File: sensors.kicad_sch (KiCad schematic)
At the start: 0 parts

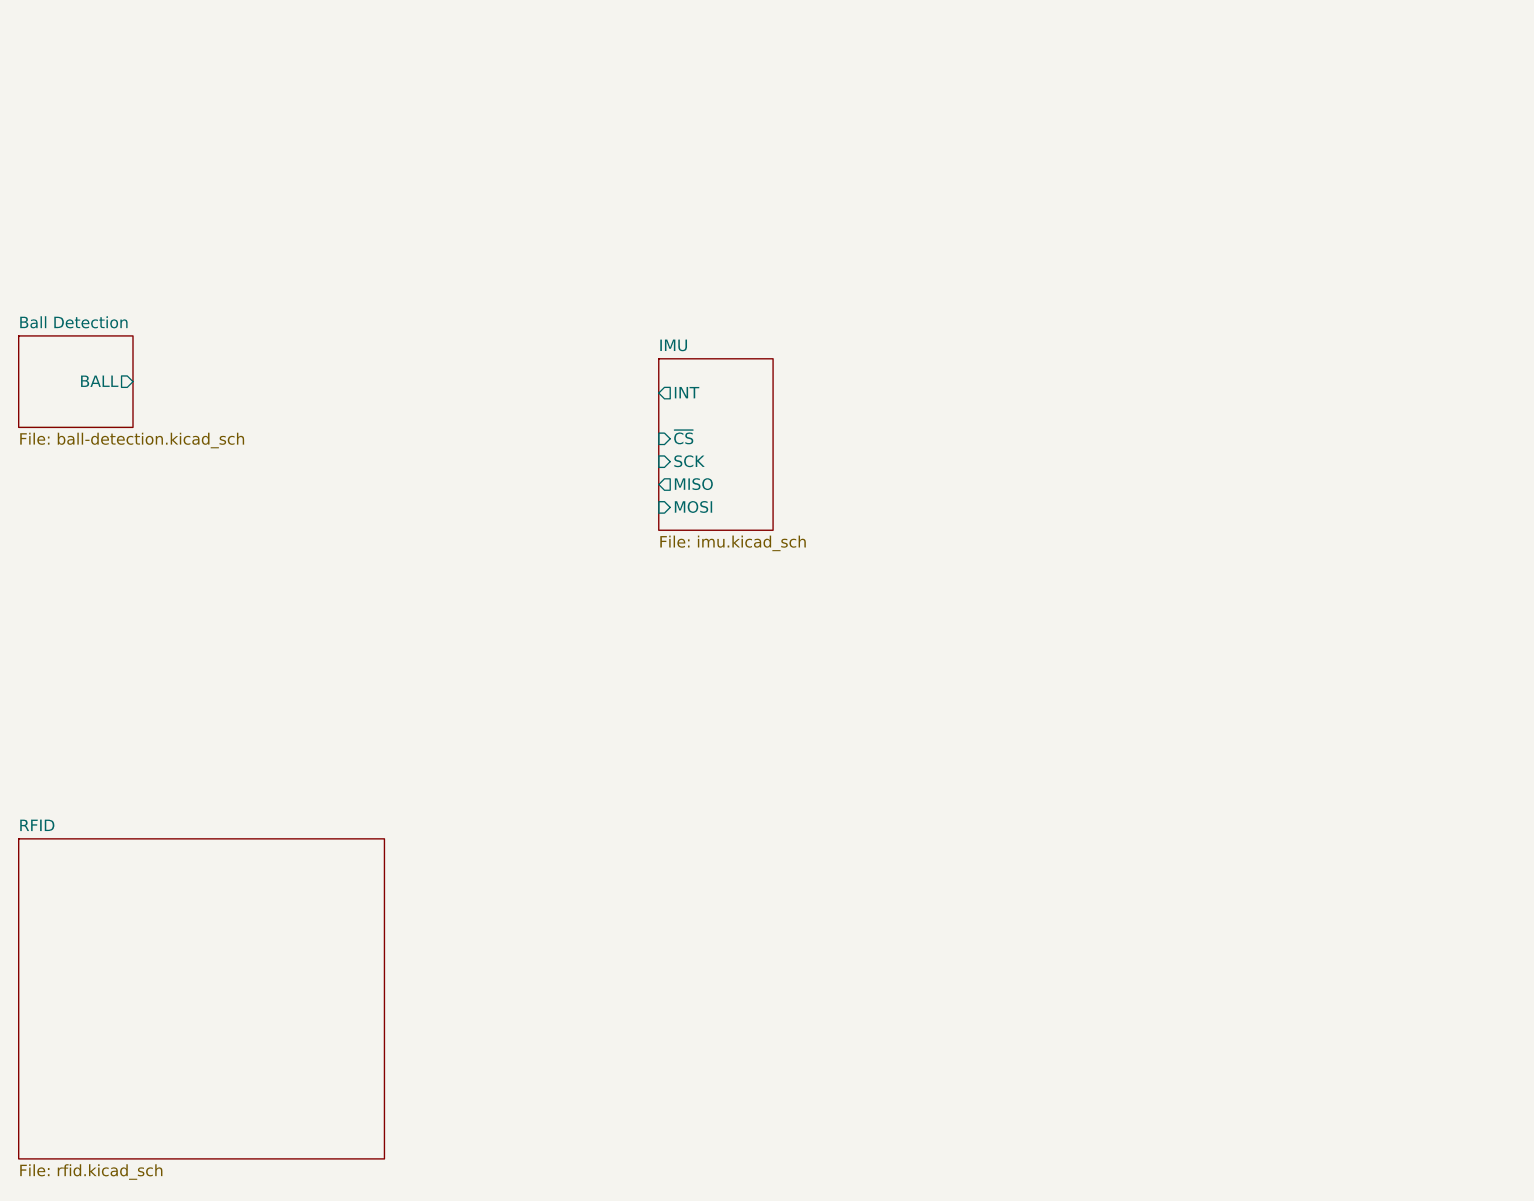
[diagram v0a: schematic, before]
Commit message: Move sensors to one sheet.
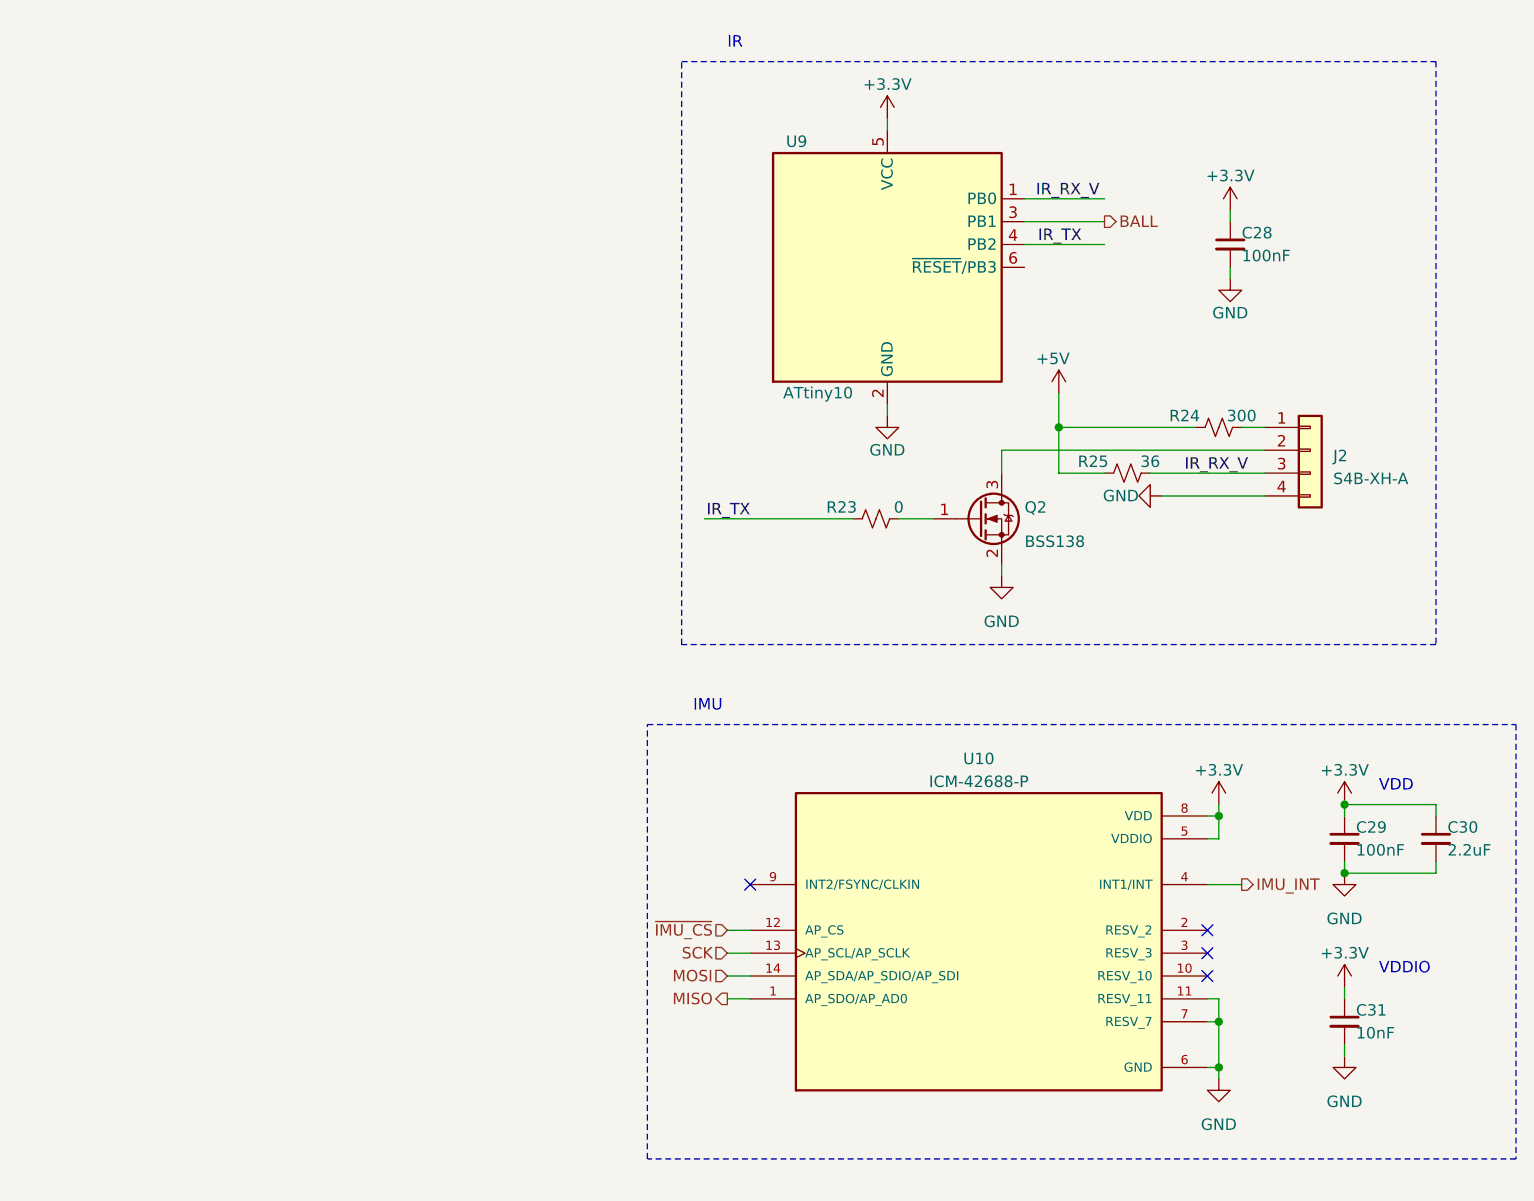
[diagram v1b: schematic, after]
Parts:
- added C28, C29: 100nF, symbol Device:C_Small
- added C30: 2.2uF, symbol Device:C_Small
- added C31: 10nF, symbol Device:C_Small
- added J2: S4B-XH-A, symbol Connector_Generic:Conn_01x04
- added Q2: BSS138, Package_TO_SOT_SMD:SOT-23, symbol Transistor_FET:BSS138
- added R23: 0, symbol Device:R_Small_US
- added R24: 300, symbol Device:R_Small_US
- added R25: 36, symbol Device:R_Small_US
- added U10: ICM-42688-P, ICM-42688-P:PQFN50P300X250X97-14N, symbol ICM-42688-P:ICM-42688-P
- added U9: ATtiny10, Package_TO_SOT_SMD:SOT-23-6, symbol MCU_Microchip_ATtiny:ATtiny10-TS
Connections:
- new net: J2.1 (Pin_1), R24.2
- new net: J2.2 (Pin_2), Q2.3 (D)
- new net: Q2.1 (G), R23.2
- new net +3.3V: C28.1, C29.1, C30.1, C31.1, U10.5 (VDDIO), U10.8 (VDD), U9.5 (VCC)
- new net +5V: R24.1, R25.1
- new net BALL: U9.3 (PB1)
- new net GND: C28.2, C29.2, C30.2, C31.2, J2.4 (Pin_4), Q2.2 (S), U10.11 (RESV_11), U10.6 (GND), U10.7 (RESV_7), U9.2 (GND)
- new net IMU_INT: U10.4 (INT1/INT)
- new net IR_RX_V: J2.3 (Pin_3), R25.2, U9.1 (PB0)
- new net IR_TX: R23.1, U9.4 (PB2)
- new net MISO: U10.1 (AP_SDO/AP_AD0)
- new net MOSI: U10.14 (AP_SDA/AP_SDIO/AP_SDI)
- new net SCK: U10.13 (AP_SCL/AP_SCLK)
- new net ~{IMU_CS}: U10.12 (AP_CS)
- no-connect marks 0 -> 4
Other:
- removed sheet Ball Detection
- removed sheet IMU
- removed sheet RFID
- note added: "IMU"
- note added: "IR"
- note added: "VDD"
- note added: "VDDIO"

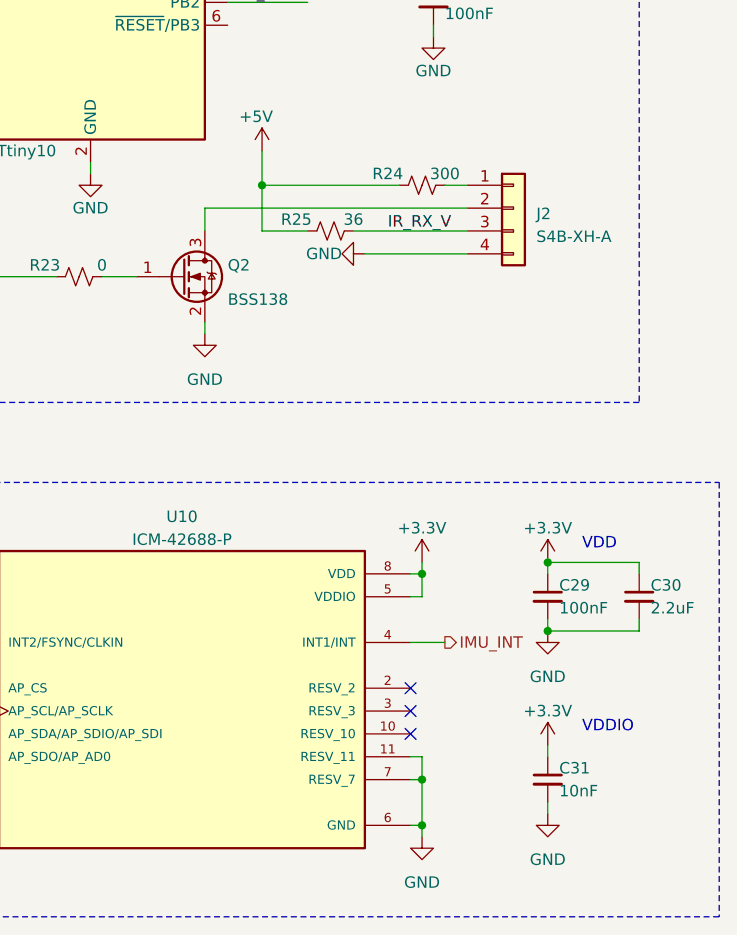
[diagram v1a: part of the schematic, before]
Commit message: Add RP2040
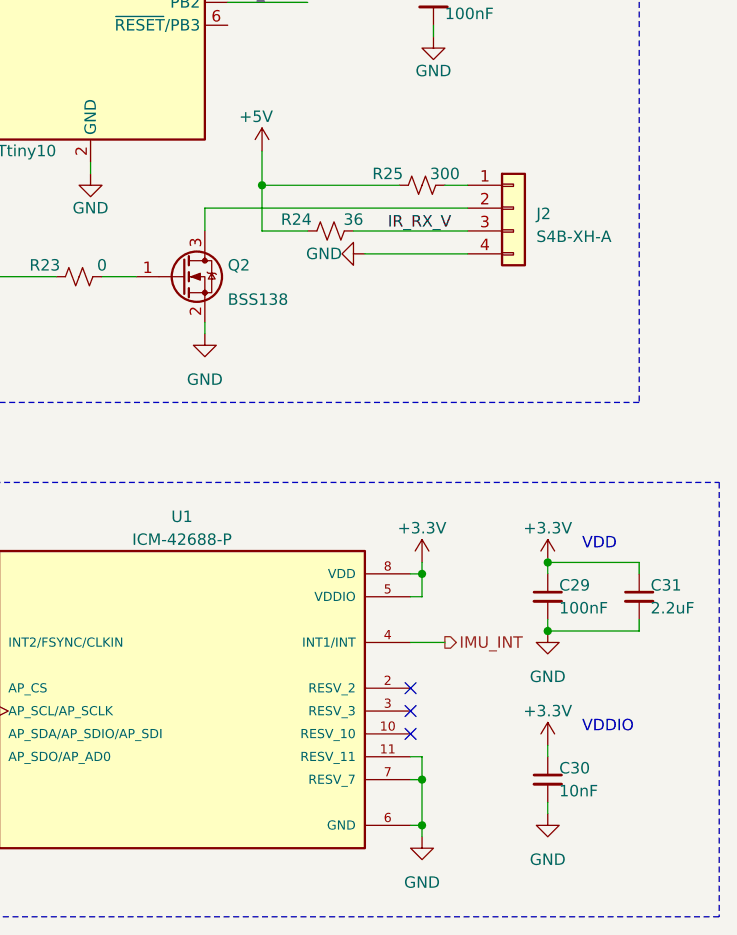
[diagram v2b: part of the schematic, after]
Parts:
- renumbered C31 to C30, C30 to C31, R25 to R24, R24 to R25, U10 to U1
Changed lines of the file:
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@@
   (symbol (lib_id "Device:R_Small_US") (at 217.17 76.2 90) (unit 1)
     (in_bom yes) (on_board yes) (dnp no)
-    (property "Reference" "R25" (at 213.36 74.93 90)
+    (property "Reference" "R24" (at 213.36 74.93 90)
       (effects (font (size 1.27 1.27)))
     )
@@
   (symbol (lib_id "Device:C_Small") (at 241.3 137.16 0) (unit 1)
     (in_bom yes) (on_board yes) (dnp no)
-    (property "Reference" "C31" (at 242.57 135.89 0)
+    (property "Reference" "C30" (at 242.57 135.89 0)
       (effects (font (size 1.27 1.27)) (justify left))
     )
@@
   (symbol (lib_id "power:+3.3V") (at 190.5 36.83 0) (unit 1)
     (in_bom yes) (on_board yes) (dnp no) (fields_autoplaced)
-    (property "Reference" "#PWR062" (at 190.5 40.64 0)
+    (property "Reference" "#PWR060" (at 190.5 40.64 0)
       (effects (font (size 1.27 1.27)) hide)
     )
@@
   (symbol (lib_id "power:GND") (at 203.2 87.63 0) (unit 1)
     (in_bom yes) (on_board yes) (dnp no) (fields_autoplaced)
-    (property "Reference" "#PWR060" (at 203.2 93.98 0)
+    (property "Reference" "#PWR062" (at 203.2 93.98 0)
       (effects (font (size 1.27 1.27)) hide)
     )
@@
   (symbol (lib_id "Device:R_Small_US") (at 227.33 71.12 90) (unit 1)
     (in_bom yes) (on_board yes) (dnp no)
-    (property "Reference" "R24" (at 223.52 69.85 90)
+    (property "Reference" "R25" (at 223.52 69.85 90)
       (effects (font (size 1.27 1.27)))
     )
@@
   (symbol (lib_id "Device:C_Small") (at 251.46 116.84 0) (unit 1)
     (in_bom yes) (on_board yes) (dnp no)
-    (property "Reference" "C30" (at 252.73 115.57 0)
+    (property "Reference" "C31" (at 252.73 115.57 0)
       (effects (font (size 1.27 1.27)) (justify left))
     )
@@
   (symbol (lib_id "ICM-42688-P:ICM-42688-P") (at 200.66 127 0) (unit 1)
     (in_bom yes) (on_board yes) (dnp no) (fields_autoplaced)
-    (property "Reference" "U10" (at 200.66 107.95 0)
+    (property "Reference" "U1" (at 200.66 107.95 0)
       (effects (font (size 1.27 1.27)))
     )
@@
   (symbol (lib_id "power:GND") (at 220.98 78.74 270) (unit 1)
     (in_bom yes) (on_board yes) (dnp no)
-    (property "Reference" "#PWR061" (at 214.63 78.74 0)
+    (property "Reference" "#PWR064" (at 214.63 78.74 0)
       (effects (font (size 1.27 1.27)) hide)
     )
@@
   (symbol (lib_id "power:GND") (at 190.5 69.85 0) (unit 1)
     (in_bom yes) (on_board yes) (dnp no)
-    (property "Reference" "#PWR064" (at 190.5 76.2 0)
-      (effects (font (size 1.27 1.27)) hide)
-    )
+    (property "Reference" "#PWR061" (at 190.5 76.2 0)
+      (effects (font (size 1.27 1.27)) hide)
+    )

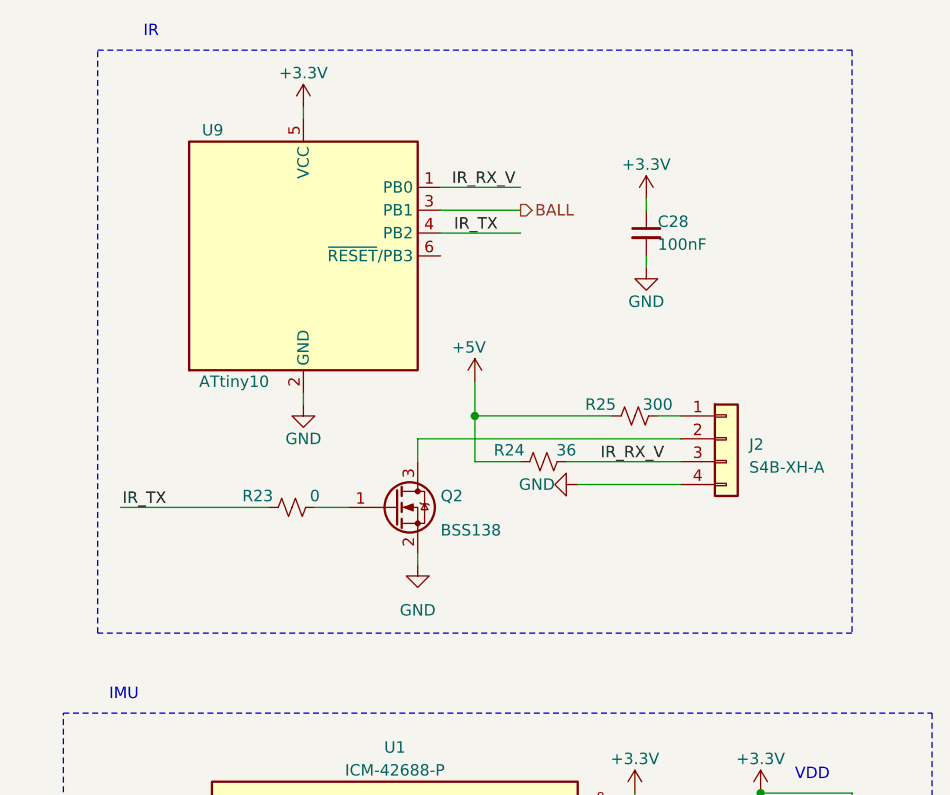
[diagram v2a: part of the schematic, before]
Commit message: Finish RP2040 connections.
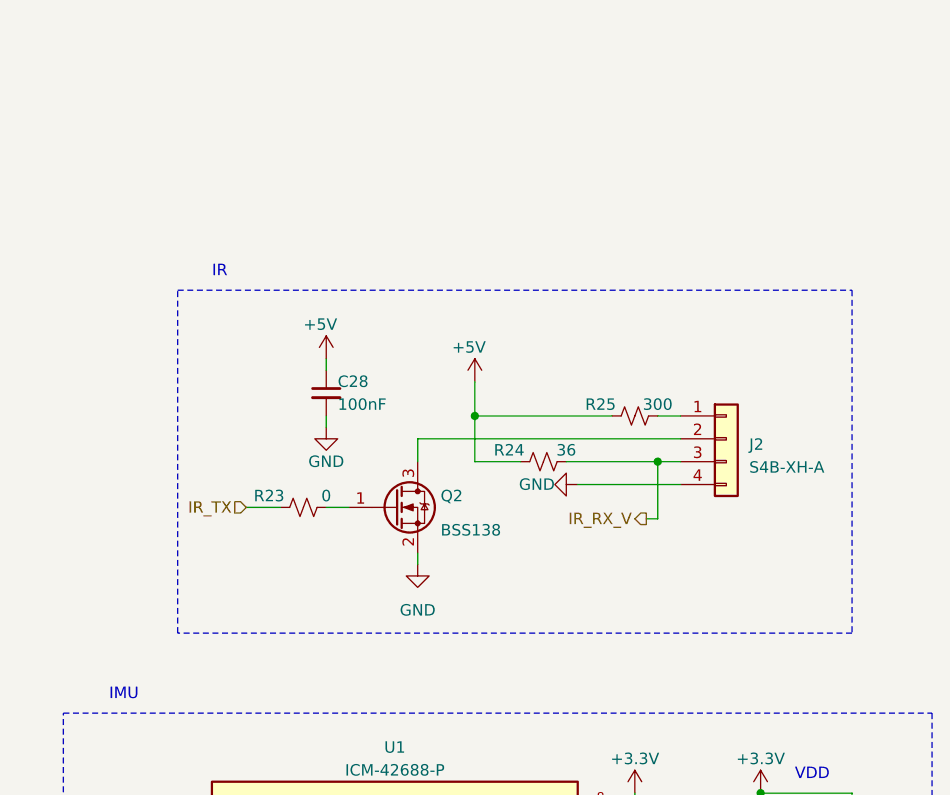
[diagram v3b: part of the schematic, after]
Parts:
- removed U9: ATtiny10, Package_TO_SOT_SMD:SOT-23-6, symbol MCU_Microchip_ATtiny:ATtiny10-TS
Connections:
- net +3.3V: no longer C28.1
- net +5V: now also C28.1
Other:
- moved on the sheet: C28, R23
